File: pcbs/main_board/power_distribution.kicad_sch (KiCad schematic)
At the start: 16 parts, among them J1 BAT1, J2 BAT2, Q1 PMOS, SW1 Power switch, U5 Step-up, U7 TP4056-42-ESOP8, U8 TC1262-33

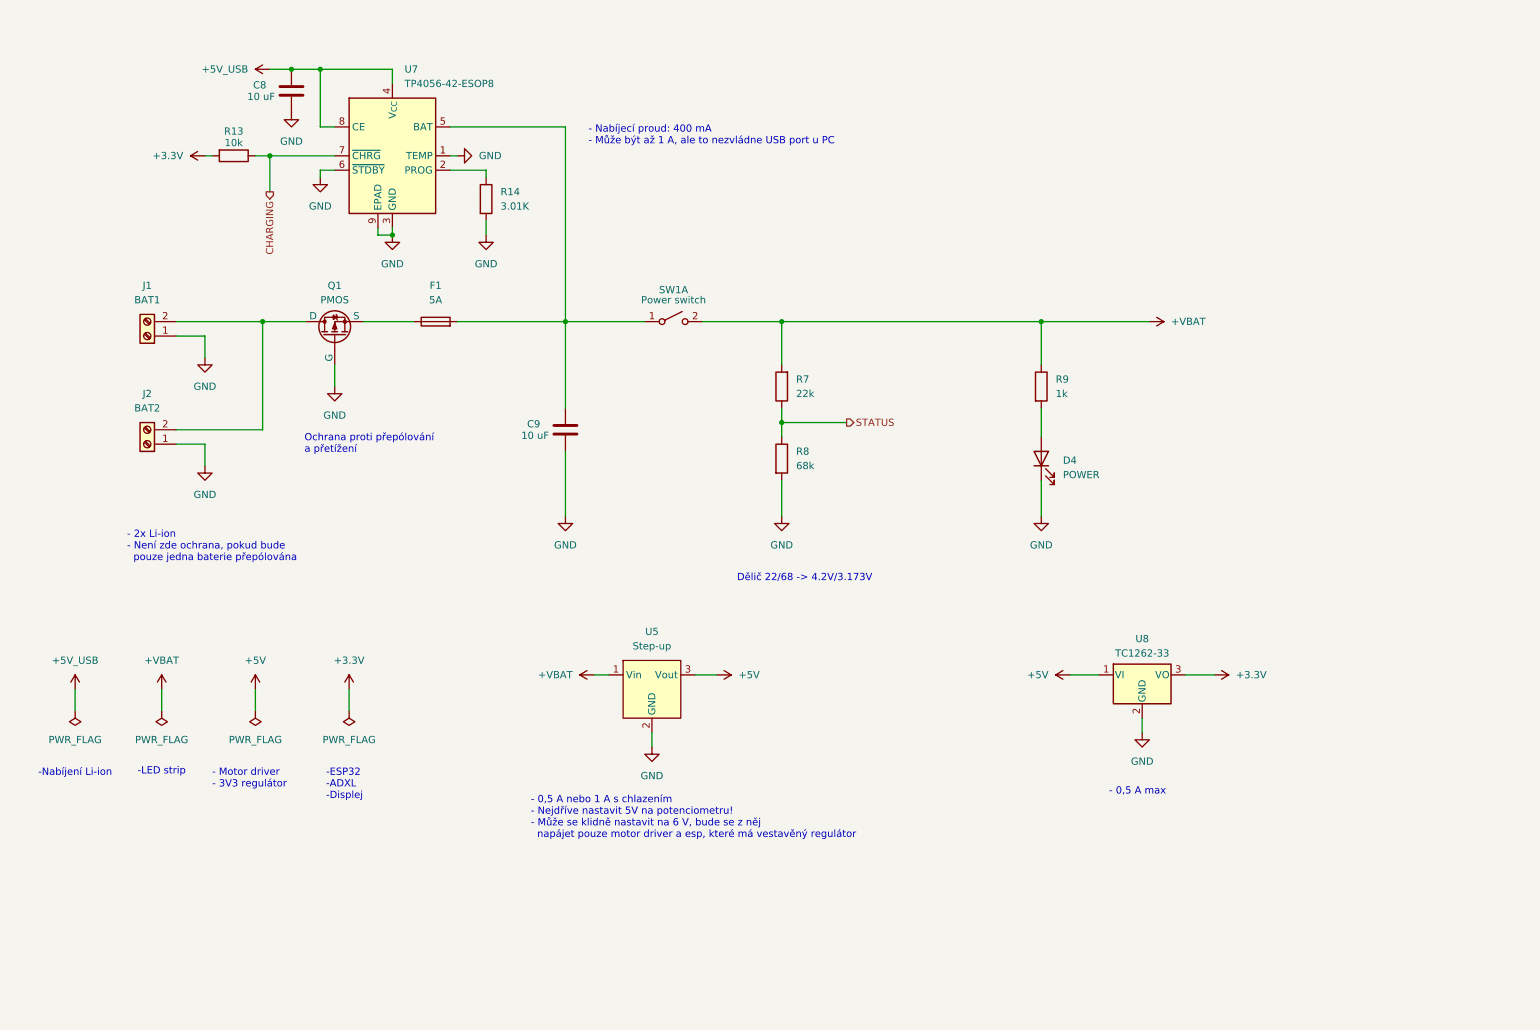
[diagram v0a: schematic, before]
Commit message: Add edge cuts and notes to pcb
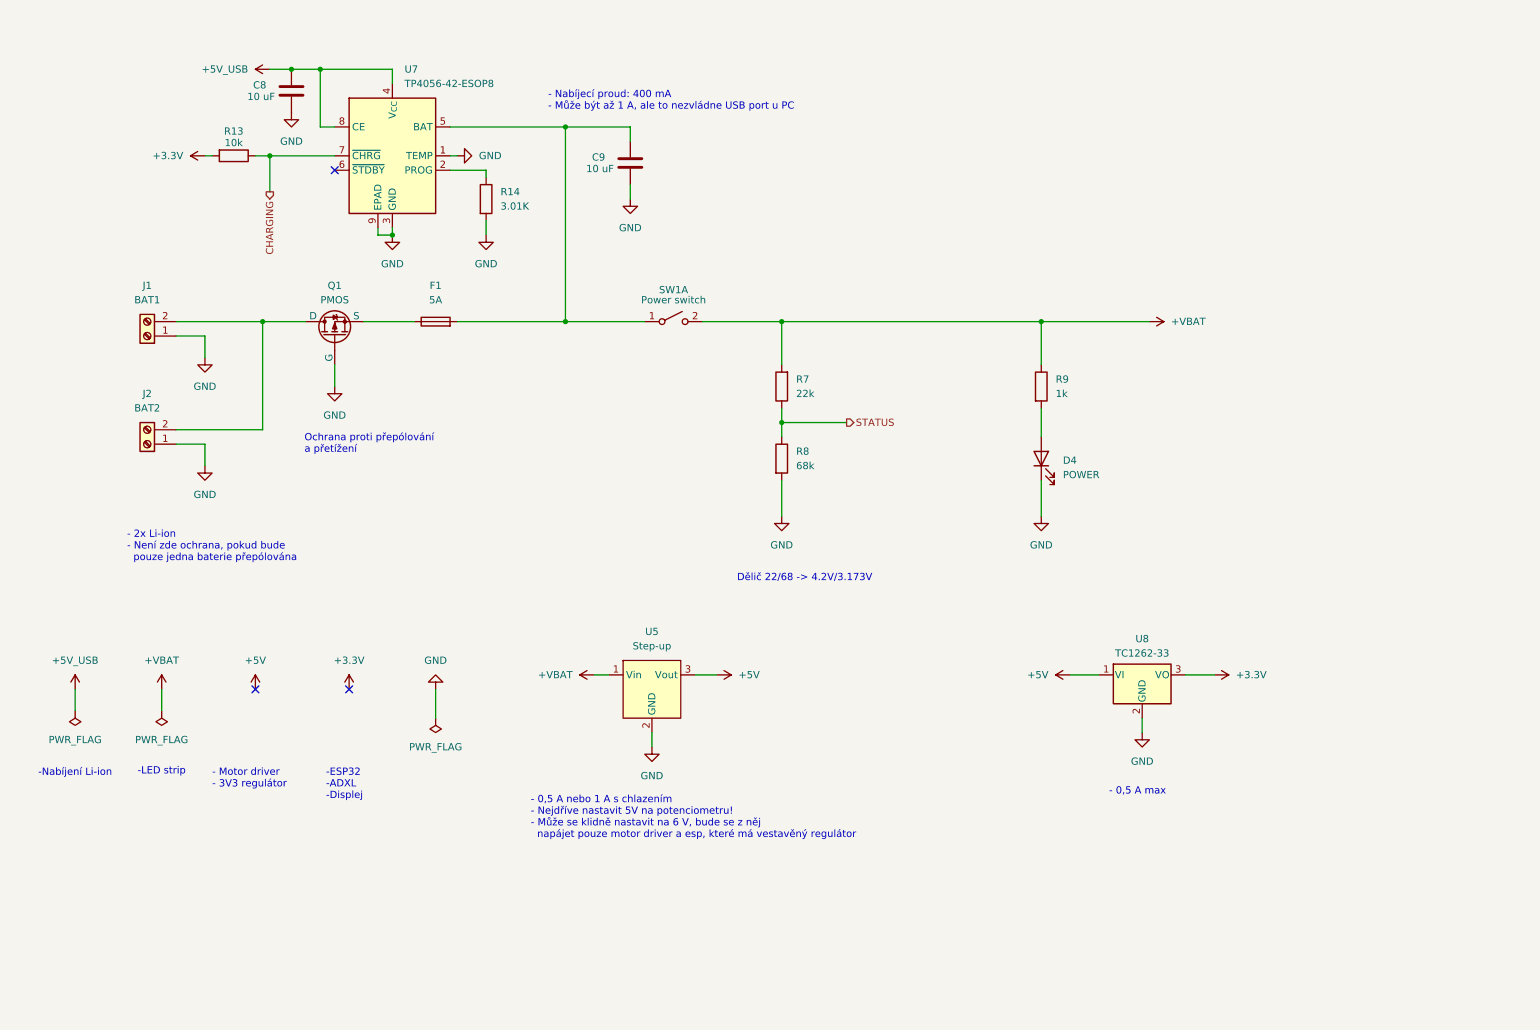
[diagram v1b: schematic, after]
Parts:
- SW1: footprint Connector_JST:JST_XH_S4B-XH-A-1_1x04_P2.50mm_Horizontal -> Connector_JST:JST_XH_S2B-XH-A-1_1x02_P2.50mm_Horizontal
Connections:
- net GND: no longer U7.6 (~{STDBY})
- no-connect marks 0 -> 3
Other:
- moved on the sheet: C9

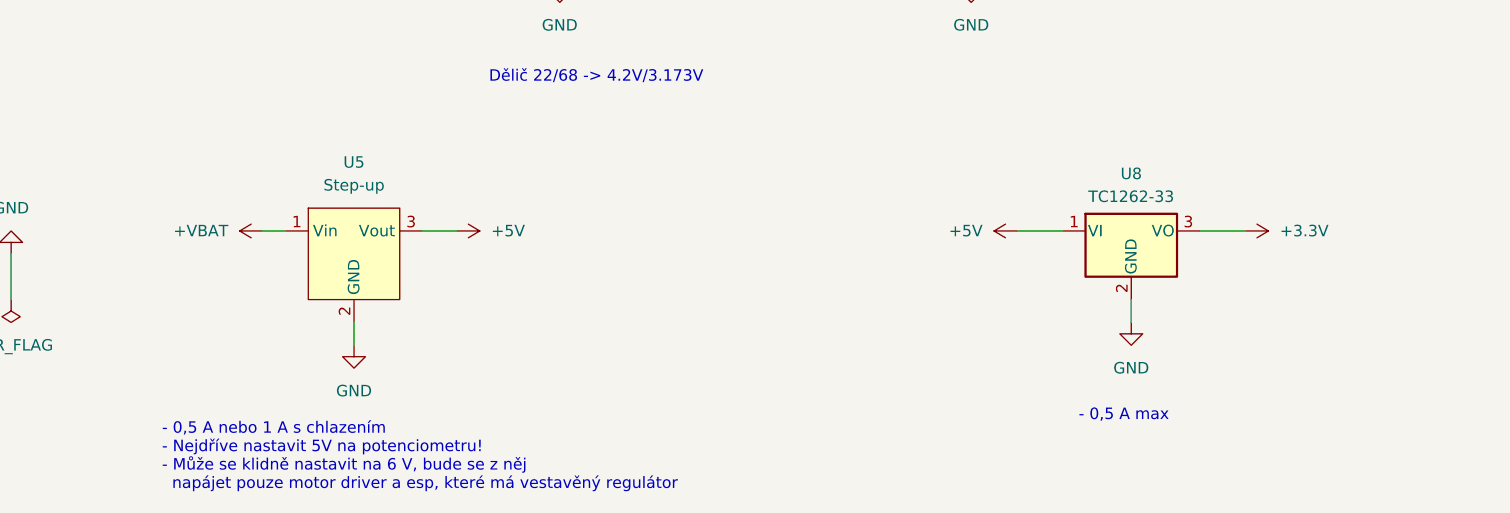
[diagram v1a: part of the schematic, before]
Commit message: Change 3V3 regulator, add level shifter for led strip
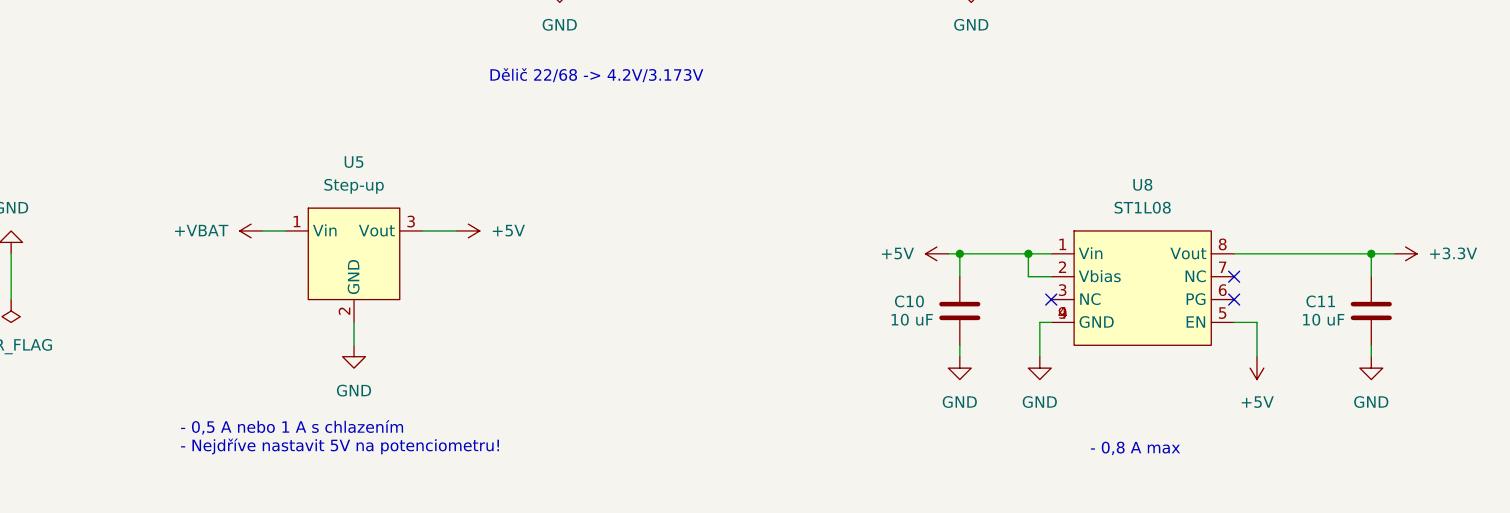
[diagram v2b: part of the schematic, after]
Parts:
- removed U8: TC1262-33, Package_TO_SOT_SMD:SOT-223-3_TabPin2, symbol Regulator_Linear:TC1262-33
- added C10, C11: 10 uF, Capacitor_SMD:C_0603_1608Metric_Pad1.08x0.95mm_HandSolder, symbol Device:C
- added U8: ST1L08, Package_DFN_QFN:DFN-8-1EP_3x2mm_P0.5mm_EP1.3x1.5mm, symbol st1l08:ST1L08
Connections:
- net +3.3V: now also C11.2, U8.8 (Vout)
- net +5V: now also C10.2, U8.1 (Vin), U8.2 (Vbias), U8.5 (EN)
- net GND: now also C10.1, C11.1, U8.4 (GND), U8.9 (GND)
- no-connect marks 3 -> 6
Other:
- note added: "- 0,5 A nebo 1 A s chlazením - Nejdříve nastavit 5V na potenciometru!"
- note added: "- 0,8 A max"
- note removed: "- 0,5 A max"
- note removed: "- 0,5 A nebo 1 A s chlazením - Nejdříve nastavit 5V na potenciometru! - Může se klidně nastavit na 6 V, bude se z něj napájet pouze motor driver a esp, které má vestavěný regulátor"

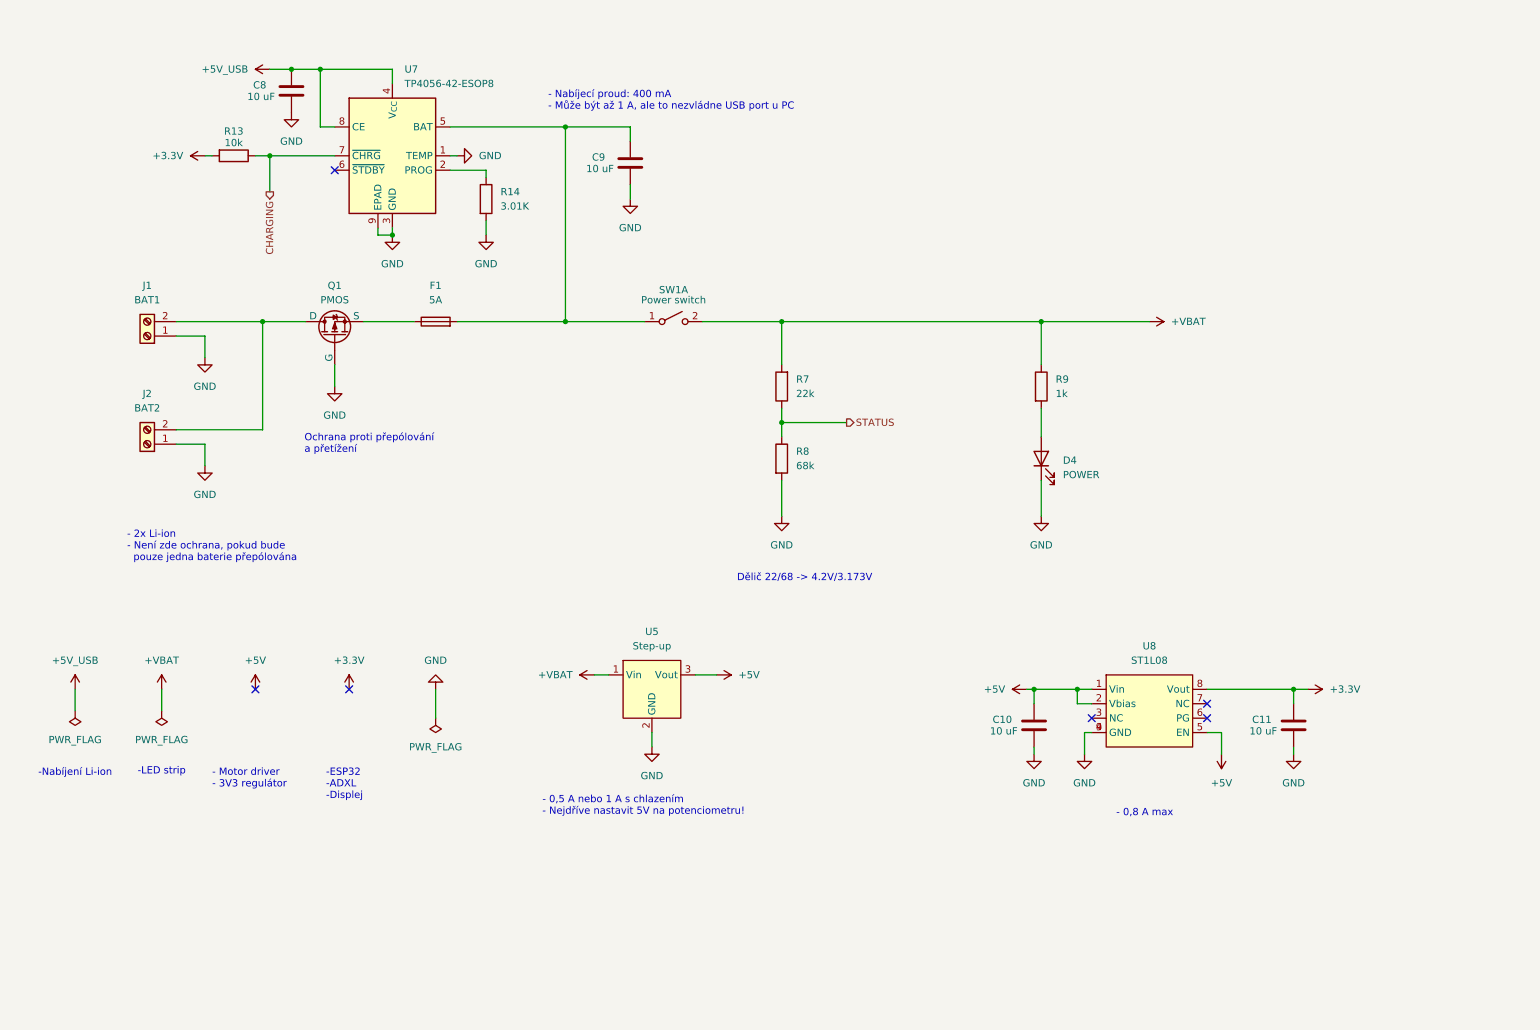
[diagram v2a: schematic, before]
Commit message: Add LED indicators
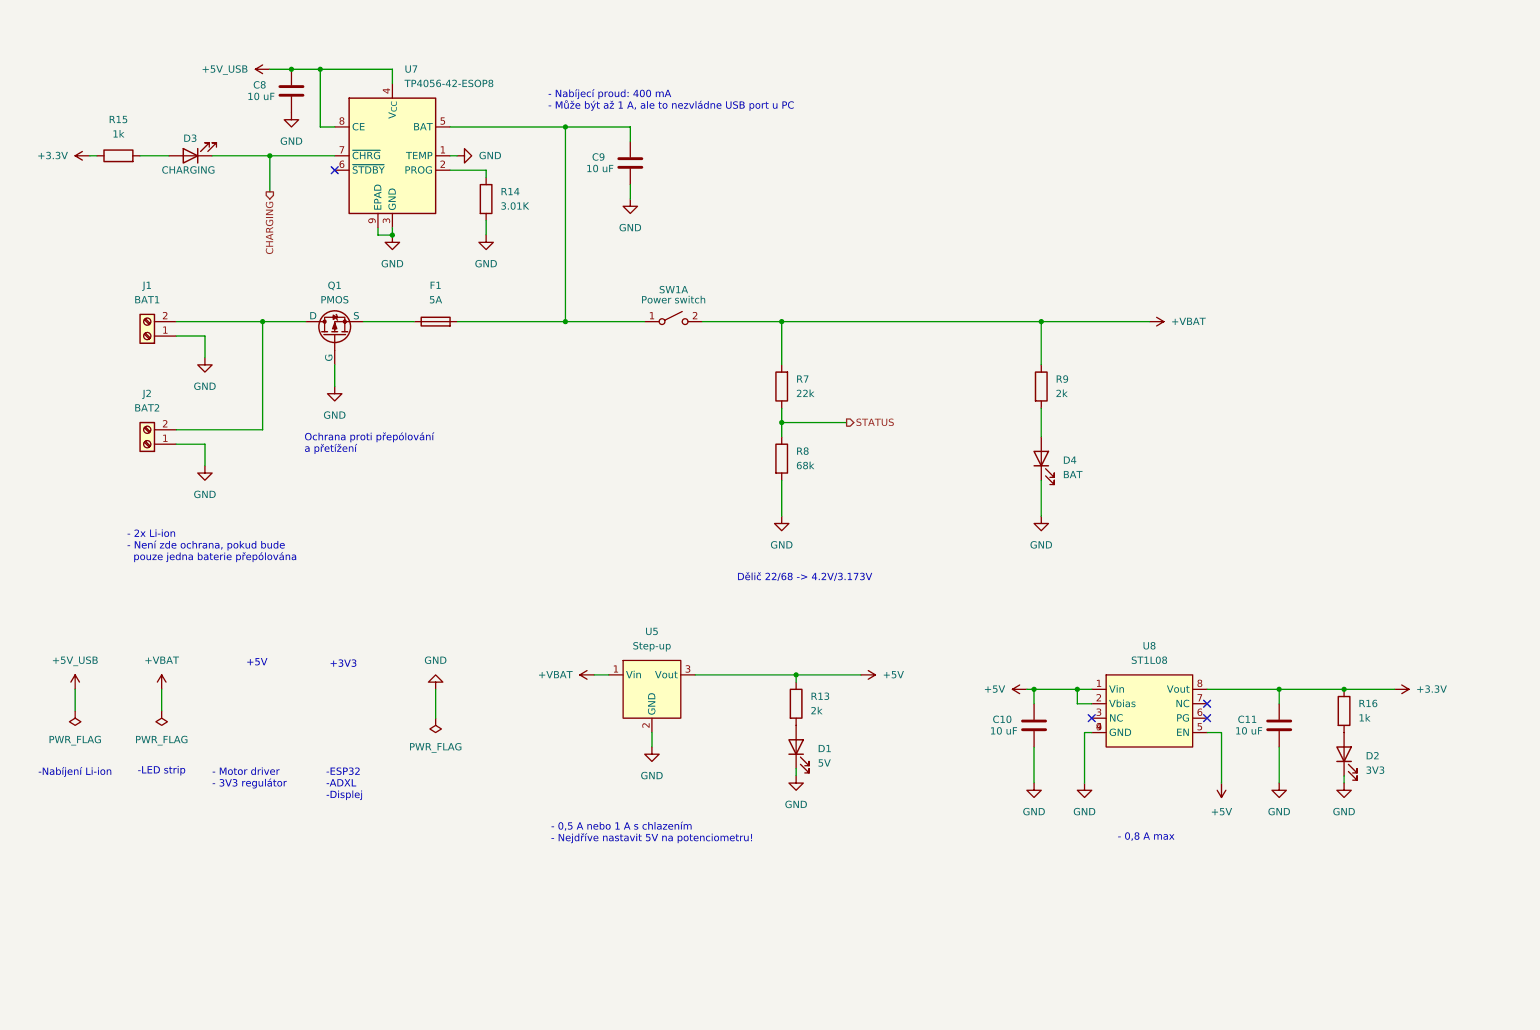
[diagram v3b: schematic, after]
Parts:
- added D1: 5V, LED_SMD:LED_0805_2012Metric_Pad1.15x1.40mm_HandSolder, symbol Device:LED
- added D2: 3V3, LED_SMD:LED_0805_2012Metric_Pad1.15x1.40mm_HandSolder, symbol Device:LED
- added D3: CHARGING, LED_SMD:LED_0805_2012Metric_Pad1.15x1.40mm_HandSolder, symbol Device:LED
- added R15, R16: 1k, Resistor_SMD:R_0603_1608Metric_Pad0.98x0.95mm_HandSolder, symbol Device:R
- D4: value POWER -> BAT
- R13: value 10k -> 2k; Manufacturer Part Number CRCW0603910KFKEAHP -> AR0603FR-072KL; Supplier Part Number 71-CRCW0603910KFKEAH -> 603-AR0603FR-072KL
- R9: value 1k -> 2k; Manufacturer Part Number CRCW06031K37FKEAHP -> AR0603FR-072KL; Supplier Part Number 71-CRCW06031K37FKEAH -> 603-AR0603FR-072KL
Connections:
- net +3.3V: now also R15.1, R16.1; no longer R13.2
- net +5V: now also R13.1
- net CHARGING: now also D3.1 (K); no longer R13.1
- net GND: now also D1.1 (K), D2.1 (K)
- new net: D3.2 (A), R15.2
- new net: D1.2 (A), R13.2
- new net: D2.2 (A), R16.2
- no-connect marks 6 -> 4
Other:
- note added: "+3V3"
- note added: "+5V"
- moved on the sheet: C11

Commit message: Add tmp BOM of main board
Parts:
- D3: Ullmanna Part Number BMCLED103 -> (none)
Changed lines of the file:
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@@
-			)
-		)
-		(property "Ullmanna Part Number" "BMCLED103 "
-			(at 45.72 41.91 0)
-			(effects
-				(font
-					(size 1.27 1.27)
-				)
-				(hide yes)
 			)
 		)
